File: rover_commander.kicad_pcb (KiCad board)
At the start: 2 copper layers, 77 x 42 mm, 75 parts, among them Q1 Crystal KX-7 25MHz, Q2 Crystal KX-7 25MHz, U1 RTL8201CP, U2 L7805ABD2T-TR, U3 H1102NLT, U4 LD1117S33TR_SOT223, U5 STM32F107RCTx, U6 TJA1040T, U7 M95160-WMN6TP

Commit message: power fix, diods replace with shottky, eeprom package, extra pull-up on reset
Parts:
- added D10: 1N5819HW-7-F, Diodes_SMD:D_SOD-123, F.Cu at (152.0, 88.4)
- added D9: 1N5819HW-7-F, Diodes_SMD:D_SOD-123, F.Cu at (139.6, 104.0)
- added J1: GS2, Connectors:GS2, F.Cu at (165.0, 96.8)
- added R28: 240, Resistors_SMD:R_0603_HandSoldering, B.Cu at (131.2, 120.4)
- added R29: 120, Resistors_SMD:R_0603_HandSoldering, B.Cu at (134.8, 118.3)
- added R30: 100k, Resistors_SMD:R_0603_HandSoldering, F.Cu at (160.9, 96.0)
- C14, C16, C17: moved to F.Cu
- D2, D4: value PMLL4148L.115 -> 1N5819HW-7-F; footprint Diodes_SMD:D_SC-80 -> Diodes_SMD:D_SOD-123
- D5: value PMLL4148L.115 -> 1N5819HW-7-F; footprint Diodes_SMD:D_SC-80_HandSoldering -> Diodes_SMD:D_SOD-123
- U4: value LD1117S33TR_SOT223 -> AMS1117-ADJ
- U7: footprint Housings_SOIC:SO-8_5.3x6.2mm_Pitch1.27mm -> Housings_SOIC:SOIC-8_3.9x4.9mm_Pitch1.27mm
- moved C14 36.1 mm to (151.4, 83.2), turned to 90 degrees
- moved C16 35.8 mm to (149.8, 83.2), turned to 90 degrees
- moved C17 32.7 mm to (148.2, 83.2), turned to 90 degrees
- moved D2 6.40 mm to (126.0, 112.2), turned to 0 degrees
- moved R2 4.77 mm to (145.6, 83.4)
- moved R23 3.97 mm to (146.2, 107.9)
- moved D4 2.75 mm to (150.6, 114.4), turned to 0 degrees
- moved U4 2.30 mm to (140.4, 117.2)
- moved C12 2.29 mm to (146.4, 117.2)
- moved R22 1.58 mm to (125.0, 107.2)
- moved D5 1.09 mm to (158.2, 114.8), turned to 180 degrees
- moved U7 1.02 mm to (157.5, 84.8)
- moved C10 0.69 mm to (131.1, 118.6)
- moved C11 0.13 mm to (153.0, 83.2)
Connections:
- C10 pad 1: /+3V3_EEPROM -> Net-(C10-Pad1)
- C11 pad 1: /+3V3_EEPROM -> /+3V3_ETH
- C12 pad 1: /+3V3_EEPROM -> Net-(C10-Pad1)
- C14 pad 1: /+3V3_EEPROM -> /+3V3_ETH
- C16 pad 1: /+3V3_EEPROM -> /+3V3_ETH
- C17 pad 1: /+3V3_EEPROM -> /+3V3_ETH
- D5 pad 2: /+3V3_EEPROM -> Net-(C10-Pad1)
- L1 pad 2: /+3V3_EEPROM -> /+3V3_ETH
- LED1 pad 2: /+3V3_EEPROM -> /+3V3_ETH
- R10 pad 1: /+3V3_EEPROM -> /+3V3_ETH
- R11 pad 1: /+3V3_EEPROM -> /+3V3_ETH
- R12 pad 1: /+3V3_EEPROM -> /+3V3_ETH
- R13 pad 1: /+3V3_EEPROM -> /+3V3_ETH
- R14 pad 1: /+3V3_EEPROM -> /+3V3_ETH
- R2 pad 2: /+3V3_EEPROM -> /+3V3_ETH
- U1 pad 14: /+3V3_EEPROM -> /+3V3_ETH
- U1 pad 27: Net-(U1-Pad27) -> (no net)
- U1 pad 37: /+3V3_EEPROM -> /+3V3_ETH
- U1 pad 38: /+3V3_EEPROM -> /+3V3_ETH
- U1 pad 39: /+3V3_EEPROM -> /+3V3_ETH
- U1 pad 41: /+3V3_EEPROM -> /+3V3_ETH
- U1 pad 43: /+3V3_EEPROM -> /+3V3_ETH
- U1 pad 48: /+3V3_EEPROM -> /+3V3_ETH
- U4 pad 1: GND -> Net-(R28-Pad1)
- U4 pad 2: /+3V3_EEPROM -> Net-(C10-Pad1)
- U5 pad 20: Net-(U5-Pad20) -> (no net)
- U5 pad 28: Net-(U5-Pad28) -> (no net)
- U5 pad 35: Net-(U5-Pad35) -> (no net)
- U5 pad 36: Net-(U5-Pad36) -> (no net)
- U5 pad 37: Net-(U5-Pad37) -> (no net)
- U5 pad 38: Net-(U5-Pad38) -> (no net)
- U5 pad 4: Net-(U5-Pad4) -> (no net)
- U5 pad 40: Net-(U5-Pad40) -> (no net)
- U5 pad 41: Net-(U5-Pad41) -> (no net)
- U5 pad 43: Net-(U5-Pad43) -> (no net)
- U5 pad 54: Net-(U5-Pad54) -> (no net)
- U5 pad 55: Net-(U5-Pad55) -> (no net)
- U5 pad 56: Net-(U5-Pad56) -> (no net)
- U5 pad 59: Net-(U5-Pad59) -> (no net)
- U5 pad 60: Net-(U5-Pad60) -> (no net)
- U5 pad 62: Net-(U5-Pad62) -> (no net)
- U5 pad 8: Net-(U5-Pad8) -> (no net)
- U7 pad 3: Net-(U7-Pad3) -> (no net)
- U7 pad 7: Net-(U7-Pad7) -> (no net)
- XP3 pad 9: /OBD2_ETH_ACT -> (no net)
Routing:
- net /+3V3_EEPROM: track 151.2 -> 10.4 mm, vias 9 -> 1
- net /+3V3_ETH: track 0.00 -> 112.1 mm, vias 0 -> 8
- net Net-(C10-Pad1): track 0.00 -> 72.3 mm, vias 0 -> 2
- net GND: track 502.2 -> 475.4 mm, vias 20 -> 15
- net /CAN_RX: track 70.6 -> 54.6 mm, vias 4 -> 2
- net Net-(J1-Pad1): track 0.00 -> 13.6 mm, vias 0 -> 1
- net /+5V: track 103.4 -> 113.7 mm, vias 2 -> 3
- net Net-(C6-Pad1): track 7.72 -> 15.1 mm, vias 1 -> 4
- net /ADC_Vbat: track 48.4 -> 54.6 mm
- net Net-(R28-Pad1): track 0.00 -> 5.80 mm
- net /USB_Vbus: track 53.0 -> 48.4 mm
- net /BUZZER: track 10.1 -> 5.97 mm
- net /ETH_MII_RX_CLK: track 43.5 -> 47.1 mm
- net /EEPROM_MISO: track 15.3 -> 18.7 mm
- net Net-(J1-Pad2): track 0.00 -> 3.07 mm
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- added copper zone on B.Cu, net Net-(C10-Pad1)
- removed copper zone on B.Cu, net /+3V3_EEPROM

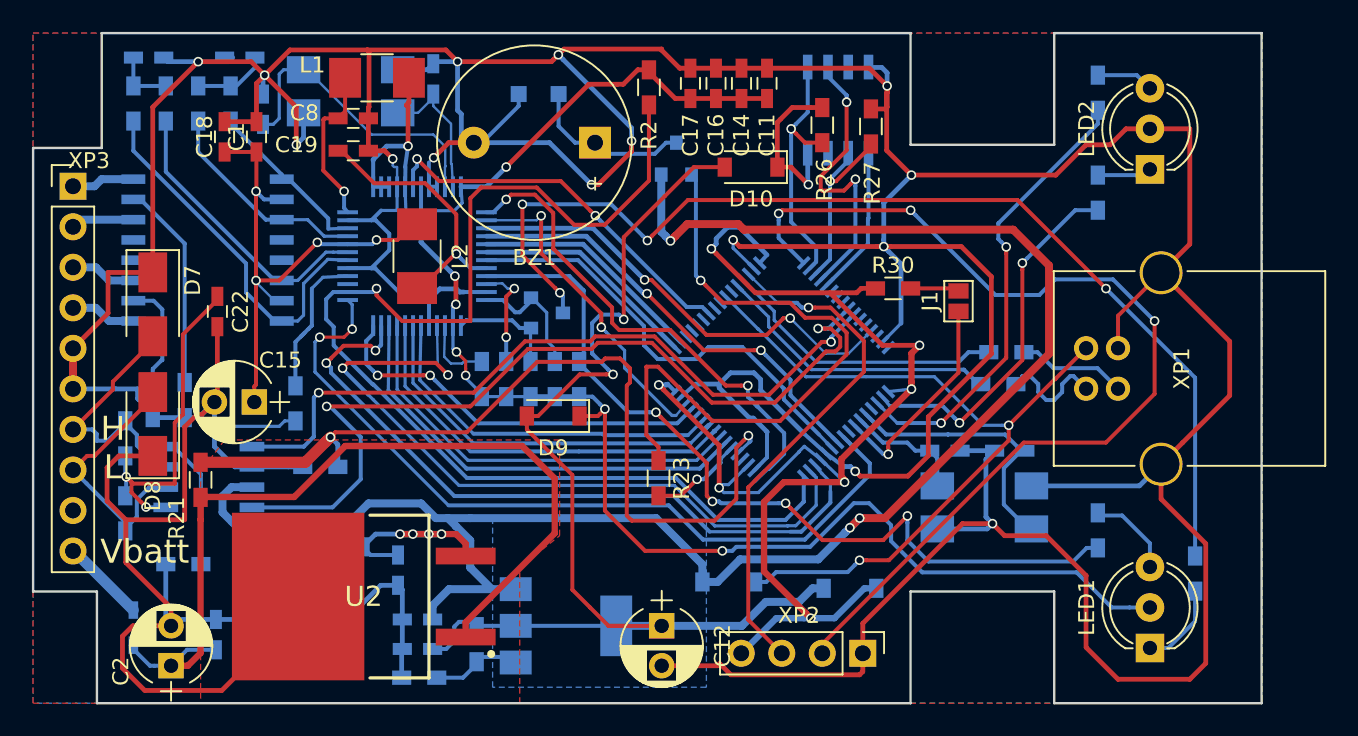
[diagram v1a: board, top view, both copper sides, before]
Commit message: fix eeprom NSS pin to correct one
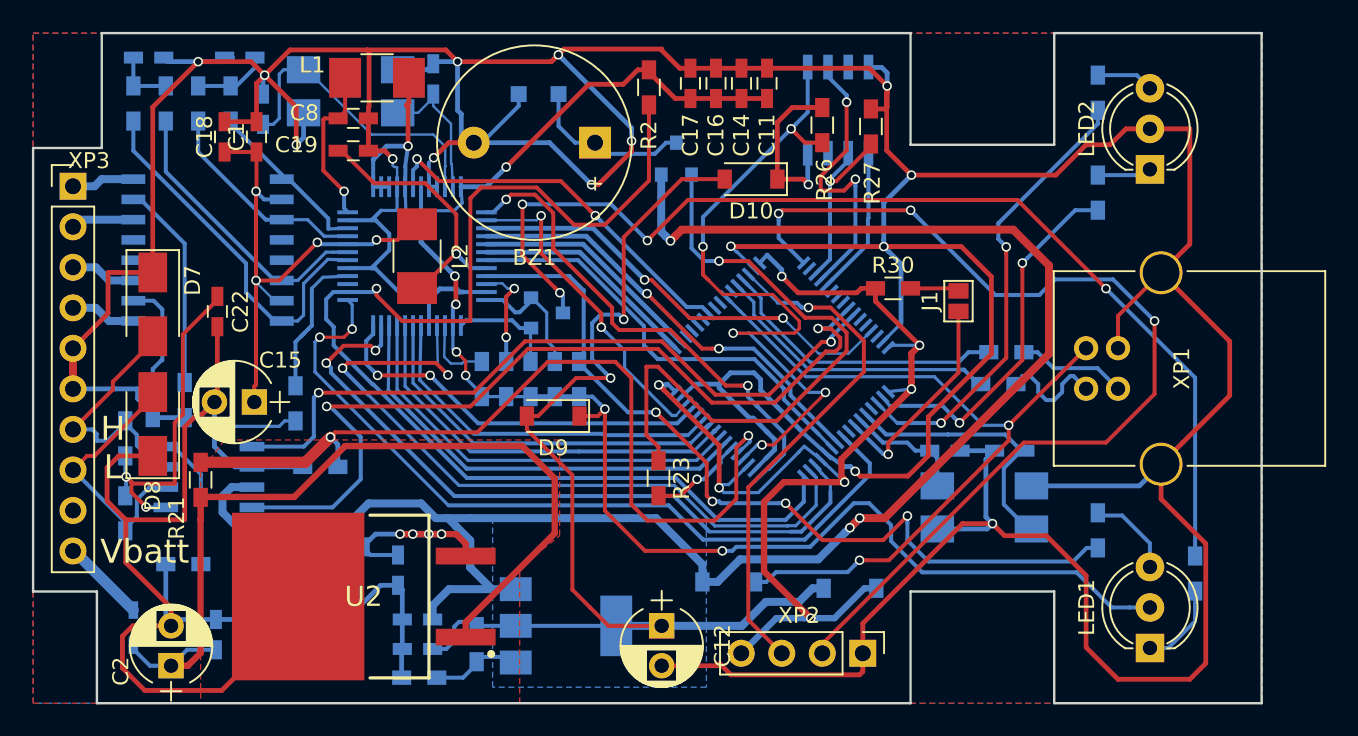
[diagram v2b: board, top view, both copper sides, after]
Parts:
- moved D10 0.75 mm to (152.0, 89.2)
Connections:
- U5 pad 20: (no net) -> /EEPROM_CS
- U5 pad 50: /EEPROM_CS -> (no net)
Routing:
- net /EEPROM_CS: track 16.2 -> 44.3 mm, vias 1 -> 5
- net /+3V3_STM: track 84.3 -> 73.6 mm
- net /ADC_Vbat: track 54.6 -> 53.4 mm
- net Net-(R23-Pad1): track 40.6 -> 39.7 mm
- net /ETH_MII_TXD3: track 28.8 -> 28.0 mm
- net /ETH_MII_TX_CLK: track 28.3 -> 27.6 mm

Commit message: fix stm32 footprint as advised in datasheet, fix libs paths
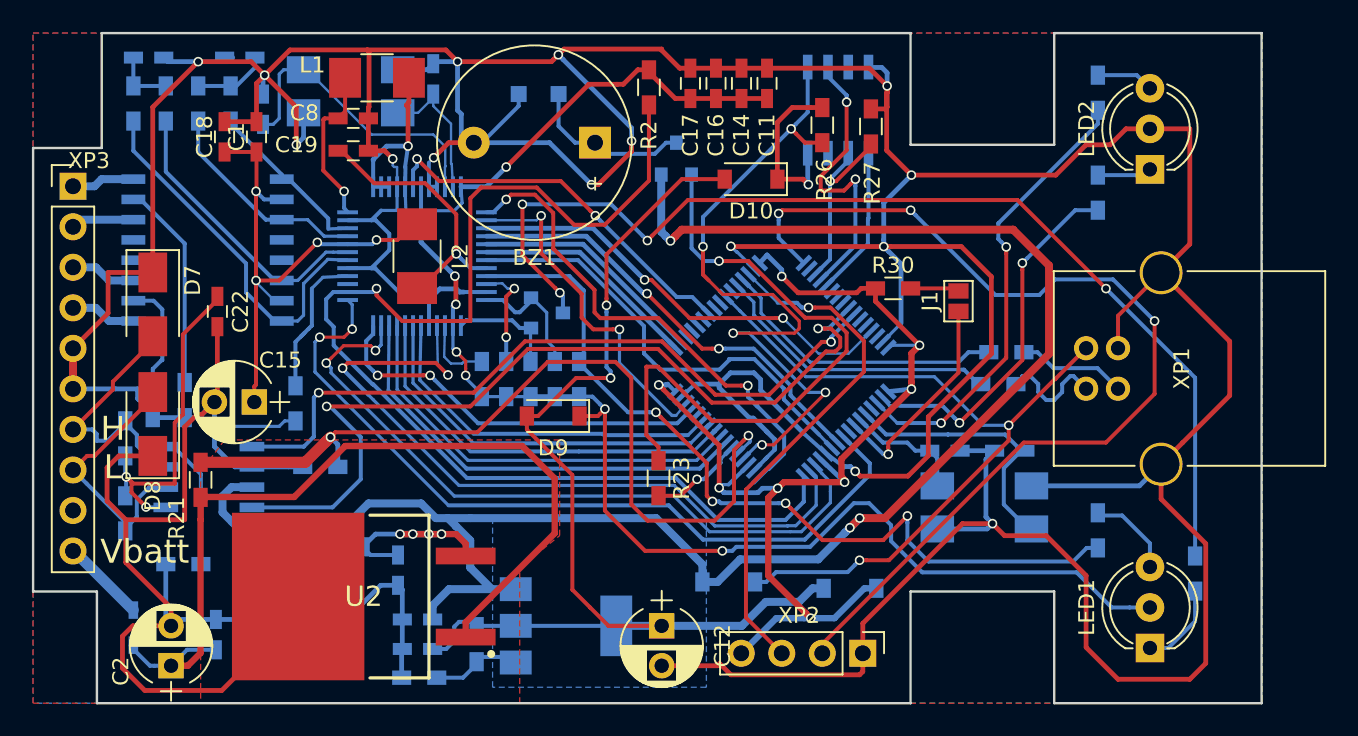
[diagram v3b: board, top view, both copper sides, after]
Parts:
- R23: value 2k -> 2k2
- U5: footprint Housings_QFP:LQFP-64_10x10mm_Pitch0.5mm -> zulljon:LQFP-64_10x10mm_Pitch0.5mm_datesheet
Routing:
- net Net-(C10-Pad1): track 71.9 -> 69.9 mm
- net /+3V3_STM: track 73.6 -> 71.8 mm, vias 7 -> 8
- net /ETH_MII_TX_EN: track 20.7 -> 21.7 mm
- net /ETH_MII_TX_CLK: track 27.6 -> 28.5 mm

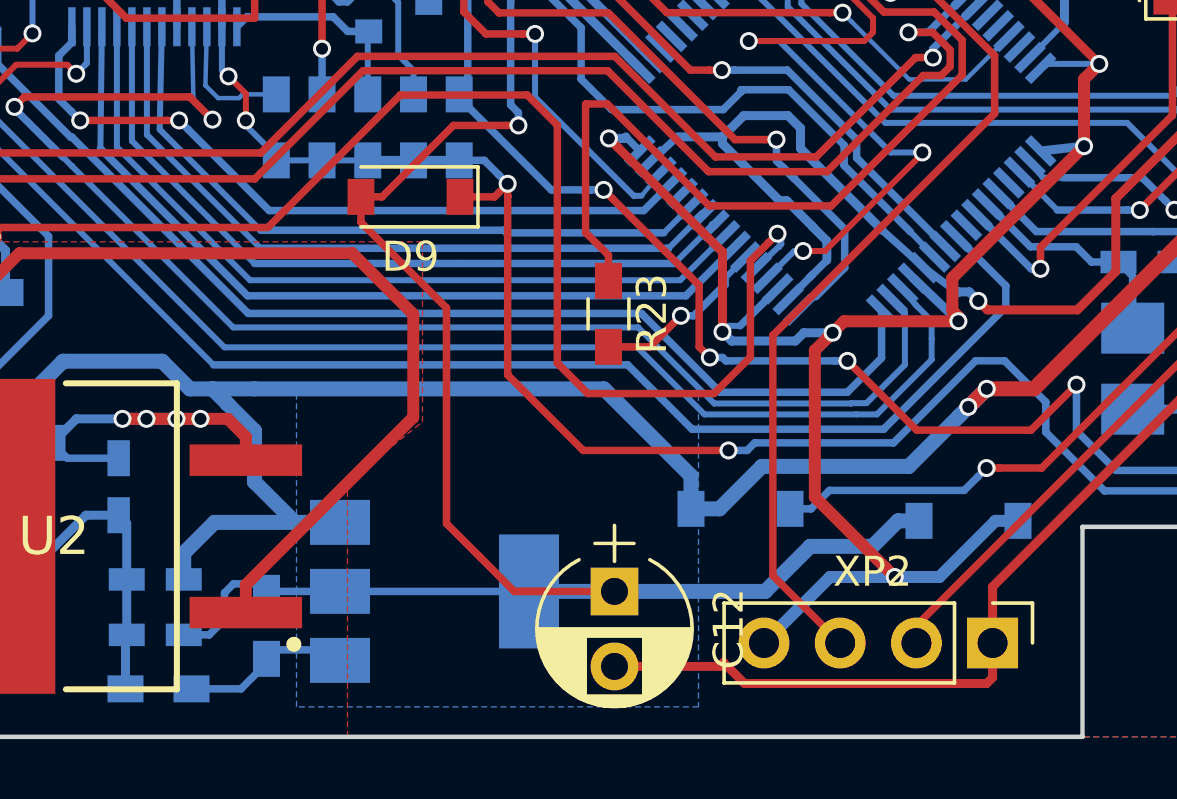
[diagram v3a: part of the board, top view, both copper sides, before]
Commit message: add blue LED on power supplier of stm32
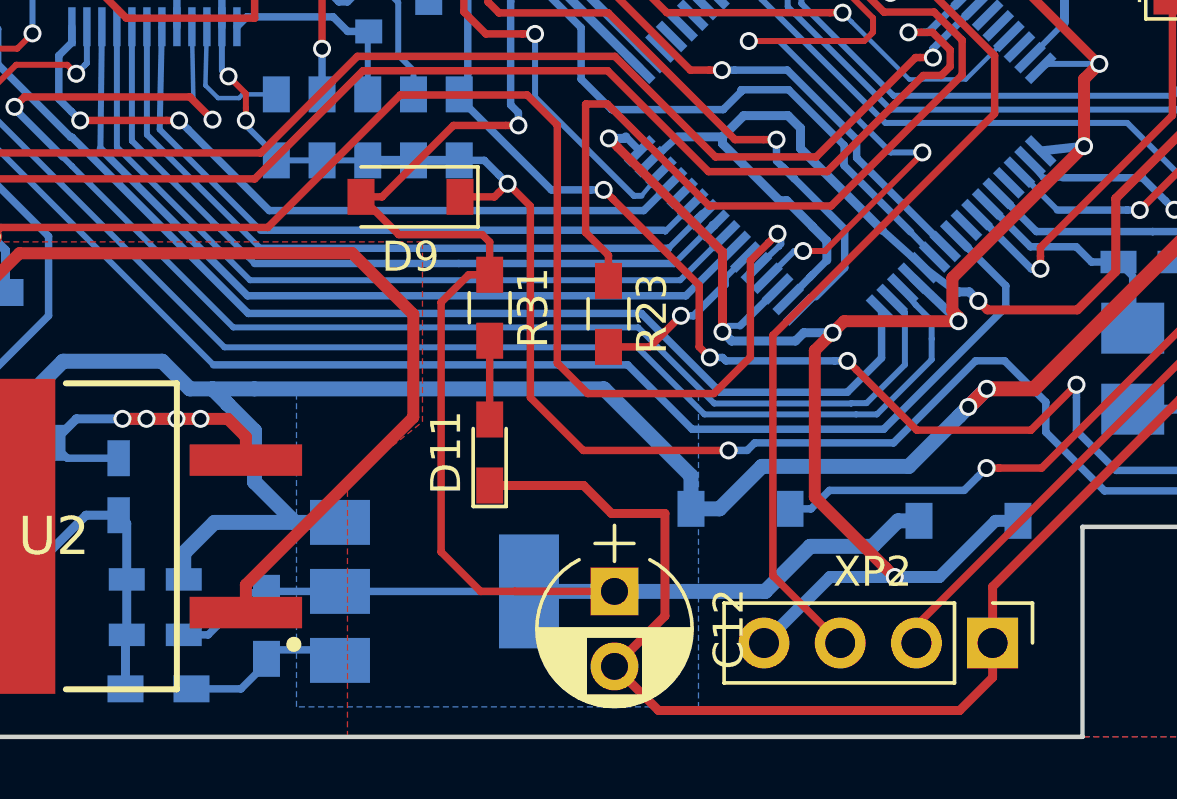
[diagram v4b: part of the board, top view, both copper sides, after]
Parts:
- added D11: LED BLUE, LEDs:LED_0603_HandSoldering, F.Cu at (142.2, 112.5)
- added R31: 1k, Resistors_SMD:R_0603_HandSoldering, F.Cu at (142.2, 107.7)
- R22: value 2.2k -> 2k2
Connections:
- net Net-(C10-Pad1) renamed /+3V65
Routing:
- net GND: track 475.6 -> 488.2 mm
- net /+3V65: track 69.9 -> 73.2 mm
- net Net-(D11-Pad2): track 0.00 -> 2.63 mm
- added copper zone on B.Cu, net Net-(C10-Pad1)
- removed copper zone on B.Cu, net /+3V65
